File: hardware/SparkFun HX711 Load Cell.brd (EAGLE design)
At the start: 30.5 x 22.9 mm, 27 parts, among them Q1 MMBT4403, U1 HX711, U7 OSHW-LOGOS

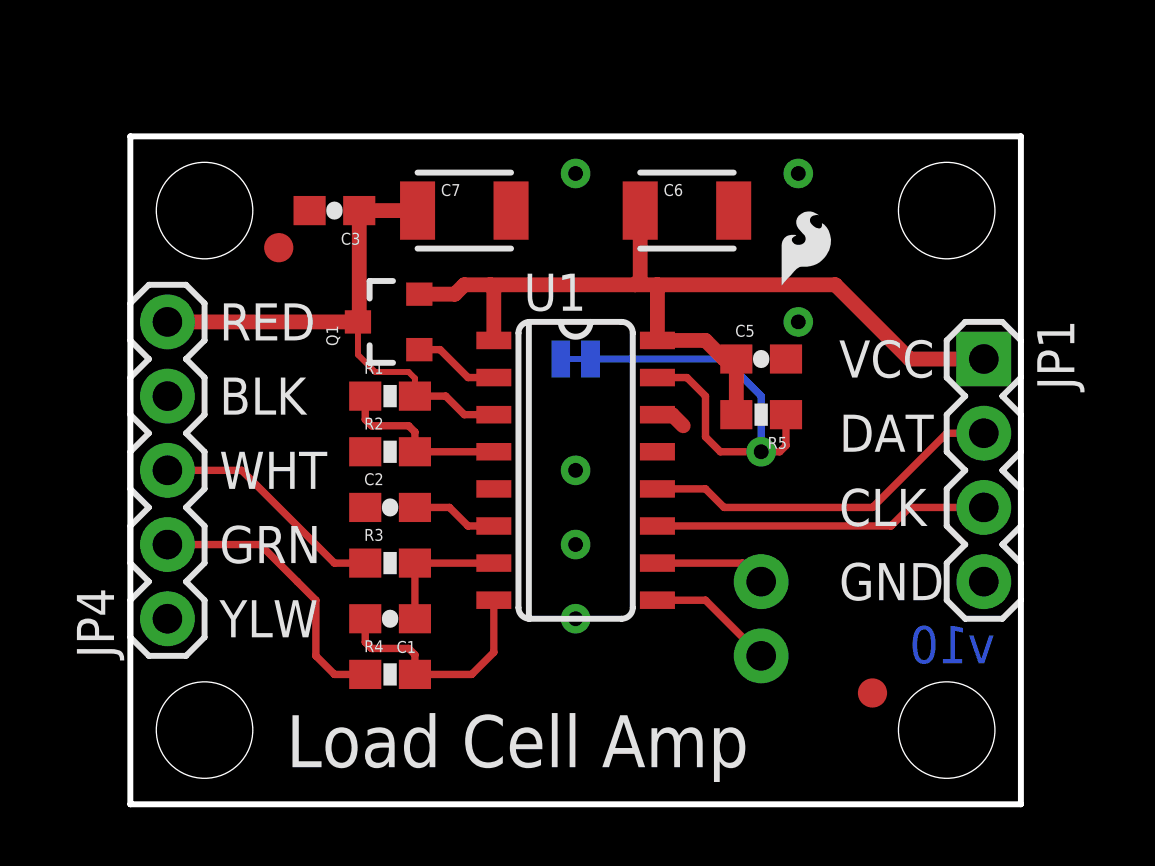
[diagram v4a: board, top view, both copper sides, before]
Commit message: Moving all headers onto horizontal grid.
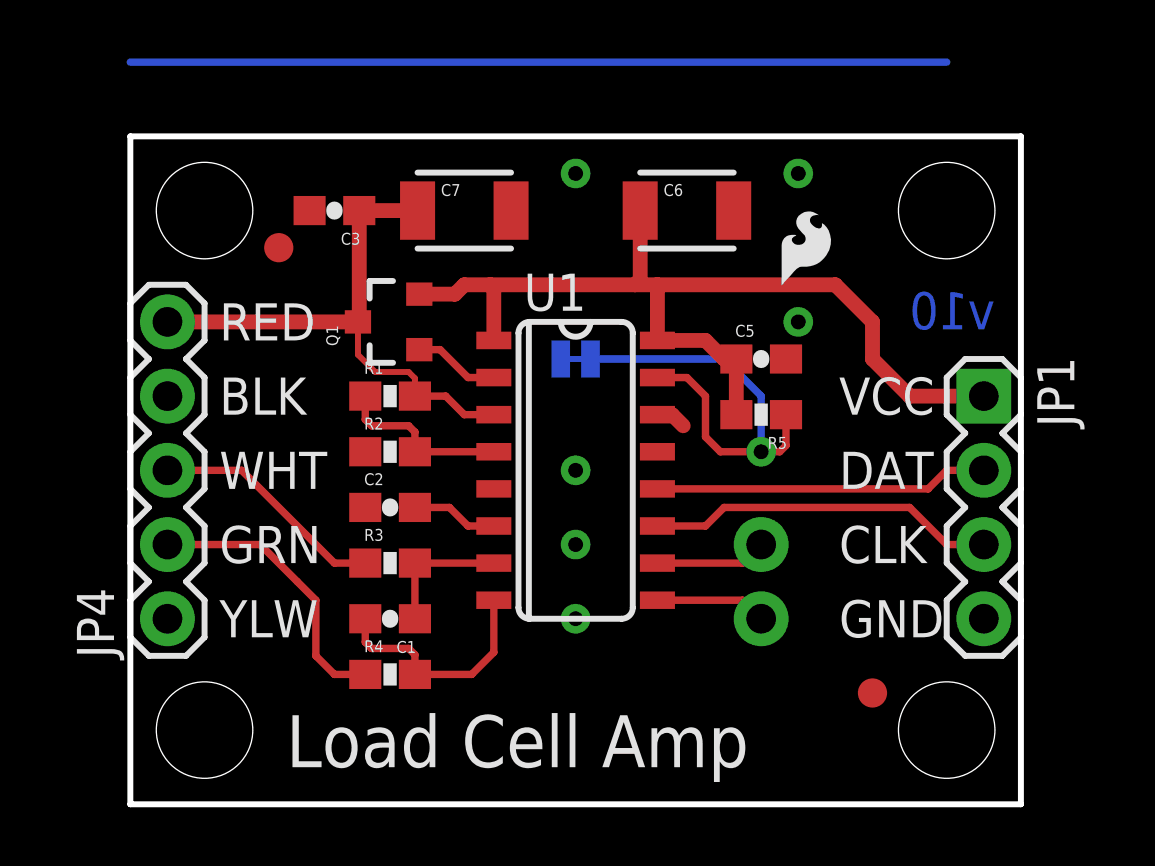
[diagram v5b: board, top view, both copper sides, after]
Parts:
- moved JP2 1.27 mm to (21.6, 8.89)
- moved JP1 1.27 mm to (29.2, 14.0)
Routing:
- net N$5: track 0.00 -> 27.9 mm
- net VCC: track 31.8 -> 33.1 mm
- net DAT: track 12.5 -> 11.4 mm
- net SCK: track 11.4 -> 12.0 mm
- net B-: track 4.34 -> 3.81 mm

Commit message: Extraneous layers removed.
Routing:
- net N$5: track 27.9 -> 0.00 mm
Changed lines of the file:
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@@
 <layer number="45" name="Holes" color="7" fill="1" visible="yes" active="yes"/>
 <layer number="46" name="Milling" color="3" fill="1" visible="no" active="yes"/>
-<layer number="47" name="Measures" color="7" fill="1" visible="no" active="yes"/>
+<layer number="47" name="Measures" color="7" fill="1" visible="yes" active="yes"/>
 <layer number="48" name="Document" color="7" fill="1" visible="no" active="yes"/>
 <layer number="49" name="Reference" color="7" fill="1" visible="no" active="yes"/>
@@
 <layer number="99" name="SpiceOrder" color="7" fill="1" visible="no" active="no"/>
 <layer number="100" name="Muster" color="7" fill="1" visible="no" active="no"/>
-<layer number="101" name="Patch_Top" color="12" fill="4" visible="no" active="yes"/>
-<layer number="102" name="Vscore" color="7" fill="1" visible="no" active="yes"/>
-<layer number="103" name="tMap" color="7" fill="1" visible="no" active="yes"/>
-<layer number="104" name="Name" color="16" fill="1" visible="no" active="yes"/>
-<layer number="105" name="tPlate" color="7" fill="1" visible="no" active="yes"/>
-<layer number="106" name="bPlate" color="7" fill="1" visible="no" active="yes"/>
-<layer number="107" name="Crop" color="7" fill="1" visible="no" active="yes"/>
-<layer number="108" name="tplace-old" color="10" fill="1" visible="no" active="yes"/>
-<layer number="109" name="ref-old" color="11" fill="1" visible="no" active="yes"/>
-<layer number="110" name="fp0" color="7" fill="1" visible="no" active="yes"/>
-<layer number="111" name="LPC17xx" color="7" fill="1" visible="no" active="yes"/>
-<layer number="112" name="tSilk" color="7" fill="1" visible="no" active="yes"/>
-<layer number="113" name="IDFDebug" color="4" fill="1" visible="no" active="yes"/>
-<layer number="116" name="Patch_BOT" color="9" fill="4" visible="no" active="yes"/>
-<layer number="121" name="_tsilk" color="7" fill="1" visible="no" active="yes"/>
-<layer number="122" name="_bsilk" color="7" fill="1" visible="no" active="yes"/>
-<layer number="123" name="tTestmark" color="7" fill="1" visible="no" active="yes"/>
-<layer number="124" name="bTestmark" color="7" fill="1" visible="no" active="yes"/>
-<layer number="125" name="_tNames" color="7" fill="1" visible="no" active="yes"/>
-<layer number="126" name="_bNames" color="7" fill="1" visible="no" active="yes"/>
-<layer number="127" name="_tValues" color="7" fill="1" visible="no" active="yes"/>
-<layer number="128" name="_bValues" color="7" fill="1" visible="no" active="yes"/>
-<layer number="131" name="tAdjust" color="7" fill="1" visible="no" active="yes"/>
-<layer number="132" name="bAdjust" color="7" fill="1" visible="no" active="yes"/>
-<layer number="144" name="Drill_legend" color="7" fill="1" visible="no" active="yes"/>
-<layer number="150" name="Notes" color="7" fill="1" visible="no" active="yes"/>
-<layer number="151" name="HeatSink" color="7" fill="1" visible="no" active="yes"/>
-<layer number="152" name="_bDocu" color="7" fill="1" visible="no" active="yes"/>
-<layer number="153" name="FabDoc1" color="7" fill="1" visible="no" active="yes"/>
-<layer number="154" name="FabDoc2" color="7" fill="1" visible="no" active="yes"/>
-<layer number="155" name="FabDoc3" color="7" fill="1" visible="no" active="yes"/>
-<layer number="199" name="Contour" color="7" fill="1" visible="no" active="yes"/>
-<layer number="200" name="200bmp" color="1" fill="10" visible="no" active="yes"/>
-<layer number="201" name="201bmp" color="2" fill="10" visible="no" active="yes"/>
-<layer number="202" name="202bmp" color="3" fill="10" visible="no" active="yes"/>
-<layer number="203" name="203bmp" color="4" fill="10" visible="no" active="yes"/>
-<layer number="204" name="204bmp" color="5" fill="10" visible="no" active="yes"/>
-<layer number="205" name="205bmp" color="6" fill="10" visible="no" active="yes"/>
-<layer number="206" name="206bmp" color="7" fill="10" visible="no" active="yes"/>
-<layer number="207" name="207bmp" color="8" fill="10" visible="no" active="yes"/>
-<layer number="208" name="208bmp" color="9" fill="10" visible="no" active="yes"/>
-<layer number="209" name="209bmp" color="7" fill="1" visible="no" active="yes"/>
-<layer number="210" name="210bmp" color="7" fill="1" visible="no" active="yes"/>
-<layer number="211" name="211bmp" color="7" fill="1" visible="no" active="yes"/>
-<layer number="212" name="212bmp" color="7" fill="1" visible="no" active="yes"/>
-<layer number="213" name="213bmp" color="7" fill="1" visible="no" active="yes"/>
-<layer number="214" name="214bmp" color="7" fill="1" visible="no" active="yes"/>
-<layer number="215" name="215bmp" color="7" fill="1" visible="no" active="yes"/>
-<layer number="216" name="216bmp" color="7" fill="1" visible="no" active="yes"/>
 <layer number="217" name="217bmp" color="18" fill="1" visible="no" active="no"/>
 <layer number="218" name="218bmp" color="19" fill="1" visible="no" active="no"/>
@@
 <layer number="223" name="223bmp" color="24" fill="1" visible="no" active="no"/>
 <layer number="224" name="224bmp" color="25" fill="1" visible="no" active="no"/>
-<layer number="248" name="Housing" color="7" fill="1" visible="no" active="yes"/>
-<layer number="249" name="Edge" color="7" fill="1" visible="no" active="yes"/>
 <layer number="250" name="Descript" color="3" fill="1" visible="no" active="no"/>
 <layer number="251" name="SMDround" color="12" fill="11" visible="no" active="no"/>
-<layer number="254" name="cooling" color="7" fill="1" visible="no" active="yes"/>
-<layer number="255" name="routoute" color="7" fill="1" visible="no" active="yes"/>
 </layers>
 <board>
@@
 <wire x1="20.955" y1="6.985" x2="21.59" y2="6.35" width="0.254" layer="1"/>
 </signal>
-<signal name="N$5">
-<wire x1="0" y1="25.4" x2="27.94" y2="25.4" width="0.254" layer="16"/>
-</signal>
 </signals>

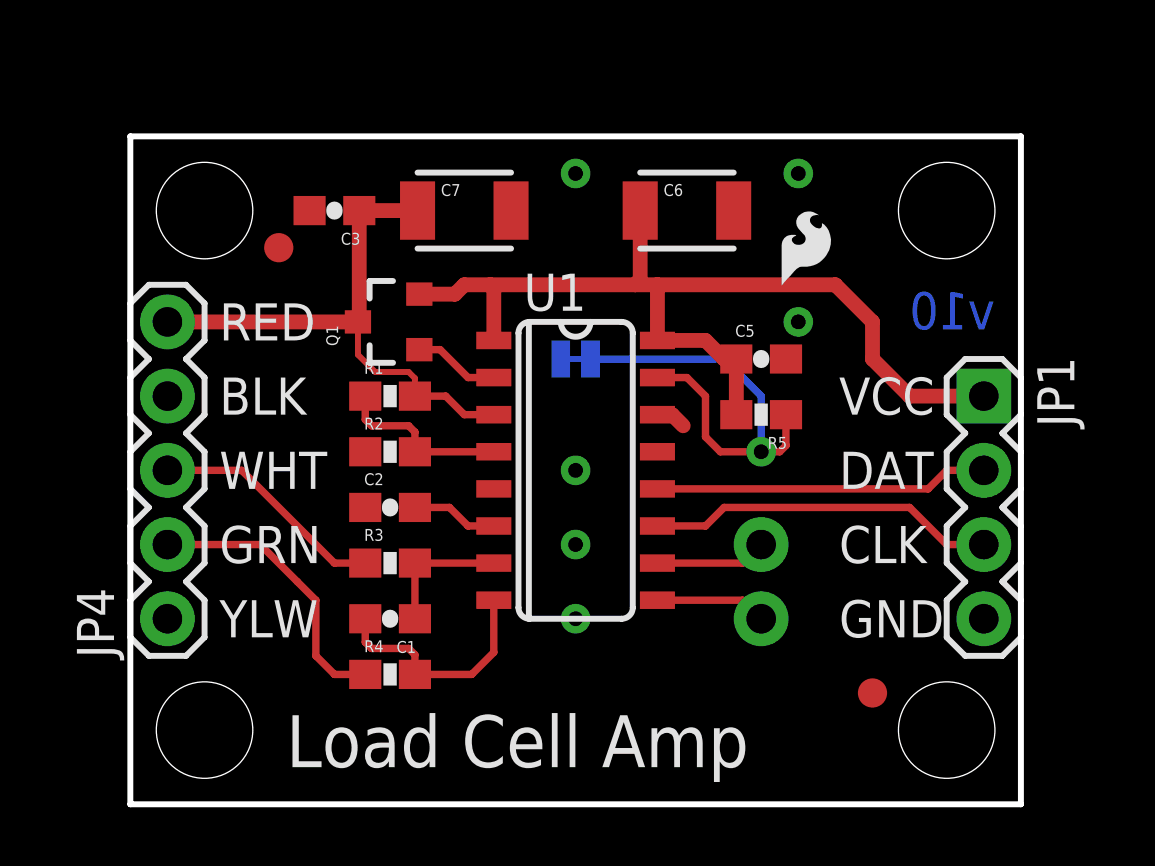
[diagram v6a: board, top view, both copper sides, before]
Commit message: Revision 11 changes
-Added 3.3uH inductor, this should allow for greater resolution in the
HX711 ADC.
-Separated analog and digital supply voltage, which allows 3.3V uCs to
communicate without additional hardware.
-Added 0.1uF cap to digital supply.
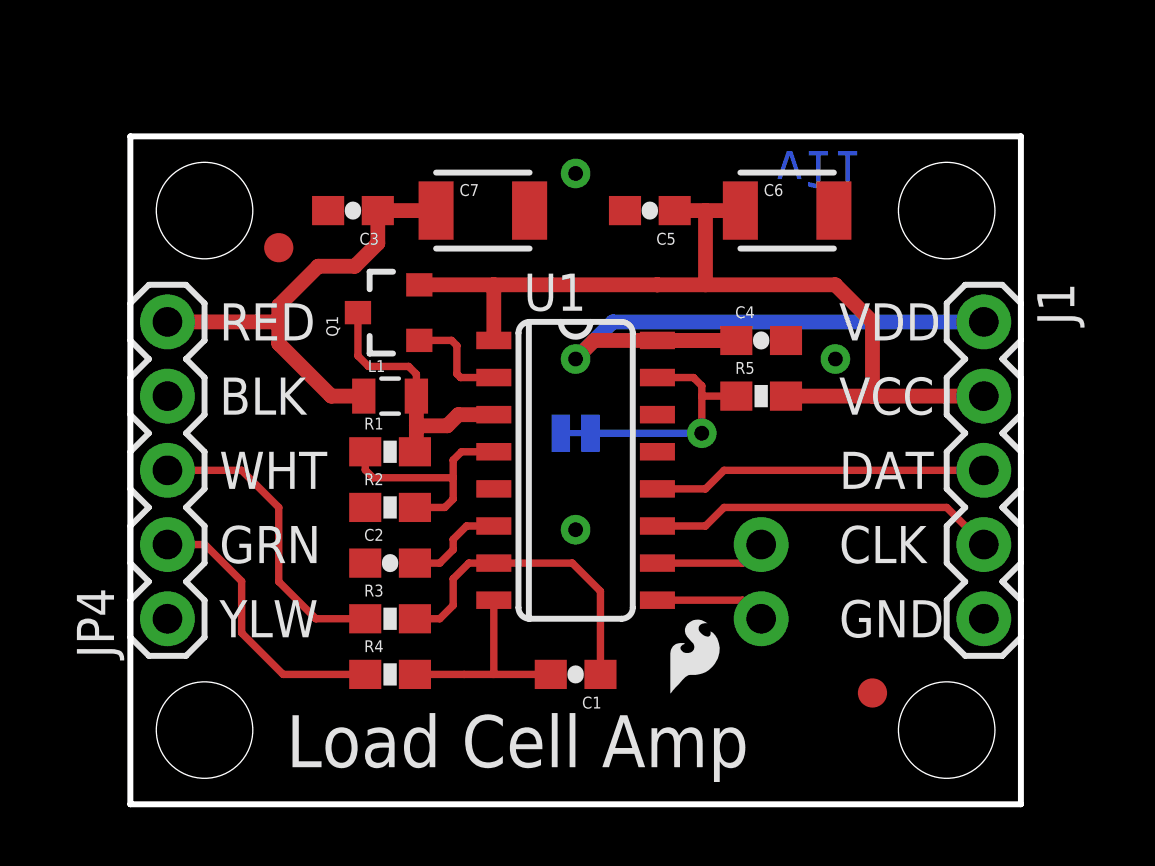
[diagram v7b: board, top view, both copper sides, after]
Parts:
- removed JP1: (no value), SparkFun-Connectors:1X04
- added C4: 0.1uF, SparkFun-Capacitors:0603-CAP
- added J1: (no value), SparkFun-Connectors:1X05
- added L1: 3.3uH, SparkFun-Passives:0805
- moved LOGO3 14.5 mm to (18.2, 3.43)
- moved C1 6.63 mm to (15.2, 4.45)
- moved C5 6.35 mm to (17.8, 20.3), turned to 180 degrees
- moved C6 3.43 mm to (22.5, 20.3)
- moved SJ2 2.54 mm to (15.2, 12.7)
- moved R1 1.91 mm to (8.89, 12.1)
- moved R3 1.91 mm to (8.89, 6.35)
- moved C2 1.90 mm to (8.89, 8.26)
- moved R2 1.90 mm to (8.89, 10.2)
- moved C3 0.63 mm to (7.62, 20.3)
- moved C7 0.63 mm to (12.1, 20.3)
- moved R5 0.63 mm to (21.6, 14.0), turned to 0 degrees
- moved Q1 0.32 mm to (8.89, 16.8)
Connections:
- new net N$5: C3.1, C7.1, JP4.5, L1.1
- new net VDD: C4.1, J1.1, U1.16
- net AVDD: now also L1.2; no longer C3.1, C7.1, JP4.5
- net DAT: now also J1.3; no longer JP1.2
- net GND: now also C4.2, J1.5; no longer JP1.4
- net SCK: now also J1.4; no longer JP1.3
- net VCC: now also J1.2; no longer JP1.1, U1.16
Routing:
- net VDD: track 0.00 -> 23.0 mm, vias 0 -> 1
- net N$5: track 0.00 -> 16.2 mm
- net AVDD: track 19.3 -> 9.25 mm
- net N$1: track 15.7 -> 8.25 mm
- net N$2: track 4.61 -> 10.9 mm
- net A-: track 8.09 -> 10.4 mm
- net N$6: track 6.05 -> 8.01 mm
- net VCC: track 33.1 -> 32.1 mm
- net N$3: track 8.15 -> 7.19 mm
- net GND: track 0.79 -> 0.00 mm, vias 6 -> 3
- net N$4: track 2.95 -> 3.64 mm
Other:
- board text added: "A. Wende"
- board text added: "Revised by:"
- board text added: "VDD"

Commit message: Revision 11 (Update)
Corrected net label from N$5 to AVDD.
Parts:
- added U$1: REVISION, SparkFun-Aesthetics:REVISION
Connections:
- net AVDD: now also C3.1, C7.1, JP4.5, L1.1; no longer L1.2, Q1.3, R1.2, U1.3
- net N$5: now also L1.2, Q1.3, R1.2, U1.3; no longer C3.1, C7.1, JP4.5, L1.1
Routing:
- net N$5: track 16.2 -> 9.25 mm
- net AVDD: track 9.25 -> 16.2 mm
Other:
- board text added: "Alex Wende"
- board text removed: "A. Wende"
- board text removed: "Revised by:"
